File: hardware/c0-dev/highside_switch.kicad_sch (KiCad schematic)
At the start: 10 parts, among them U34 TPS26600PWP

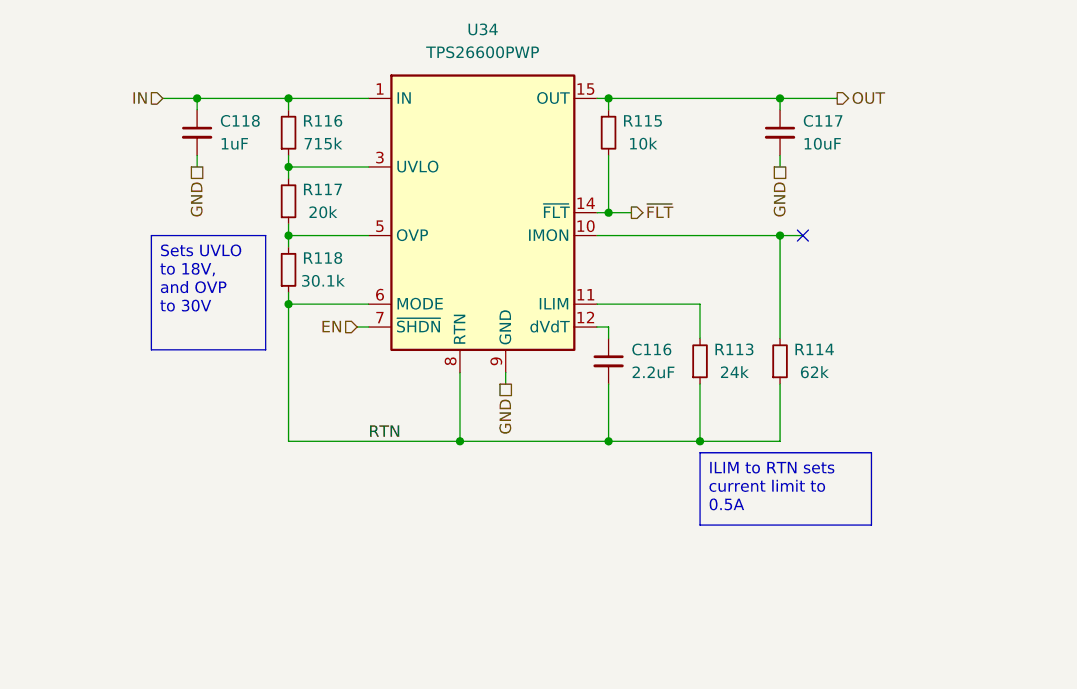
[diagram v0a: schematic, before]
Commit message: added DO
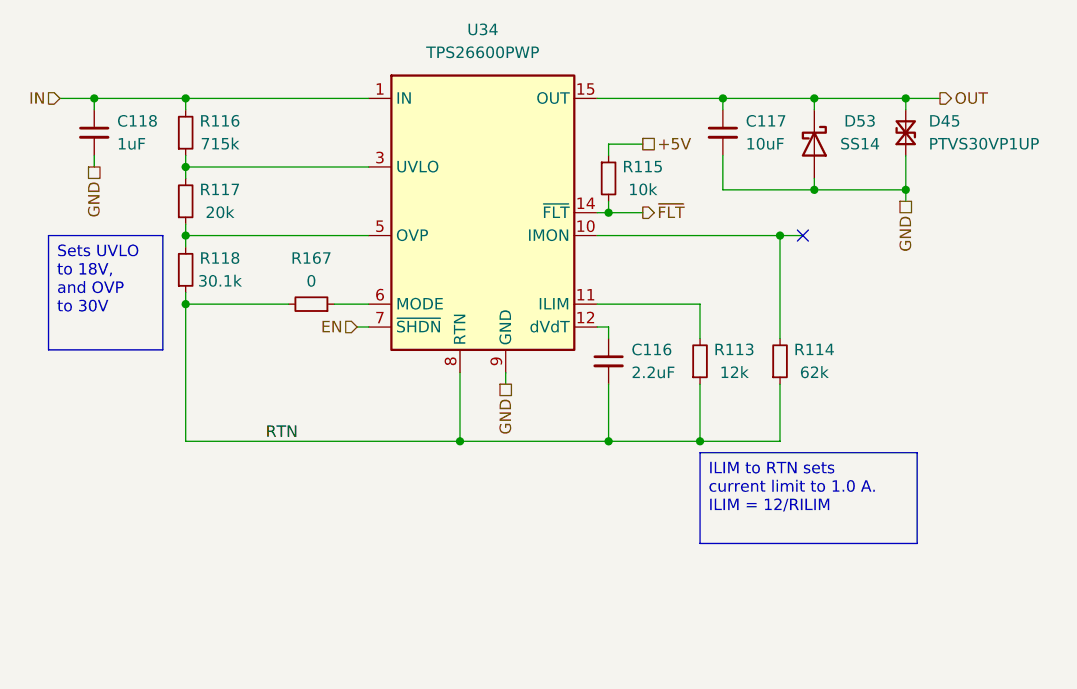
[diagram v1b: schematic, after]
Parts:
- added D45: PTVS30VP1UP, Diode_SMD:D_SOD-128, symbol Device:D_TVS_Small
- added D53: SS14, Diode_SMD:D_SMA, symbol Diode:B140-E3
- added R167: 0, Resistor_SMD:R_0402_1005Metric, symbol Device:R_Small
- R113: value 24k -> 12k
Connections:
- net GND: now also D45.1 (A1), D53.2 (A)
- net OUT: now also D45.2 (A2), D53.1 (K); no longer R115.1
- net RTN: now also R167.2; no longer U34.6 (MODE)
- new net: R167.1, U34.6 (MODE)
- new net +5V: R115.1
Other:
- moved on the sheet: C117, C118, R115, R116, R117, R118

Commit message: i2c address check
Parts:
- renumbered C118 to C122, C116 to C123, C117 to C124, D53 to D37, D45 to D38, R116 to R120, R117 to R121, R118 to R122, R167 to R123, R115 to R124, R113 to R125, R114 to R126, U34 to U36

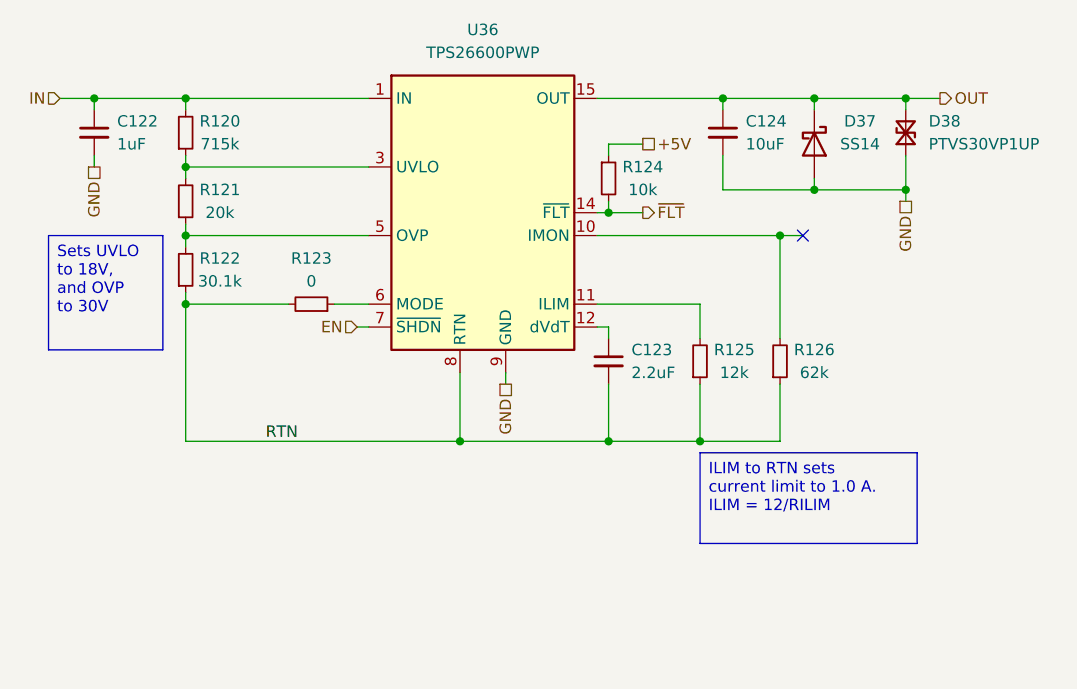
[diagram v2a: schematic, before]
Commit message: added connectors
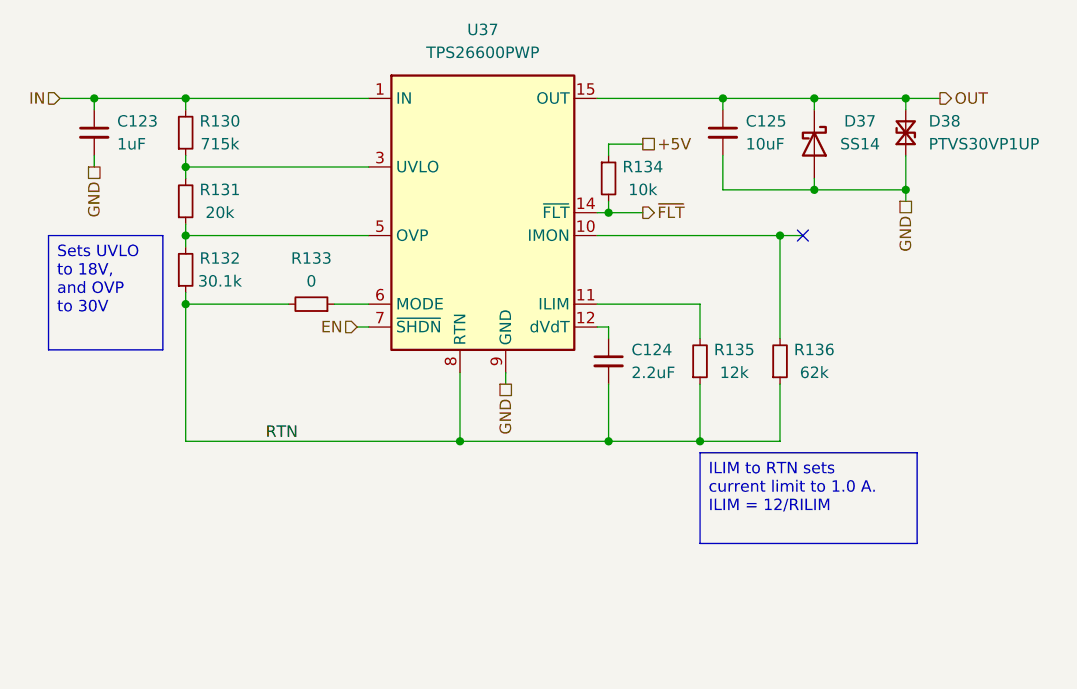
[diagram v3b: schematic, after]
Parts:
- renumbered C122 to C123, C123 to C124, C124 to C125, R120 to R130, R121 to R131, R122 to R132, R123 to R133, R124 to R134, R125 to R135, R126 to R136, U36 to U37

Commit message: added status leds
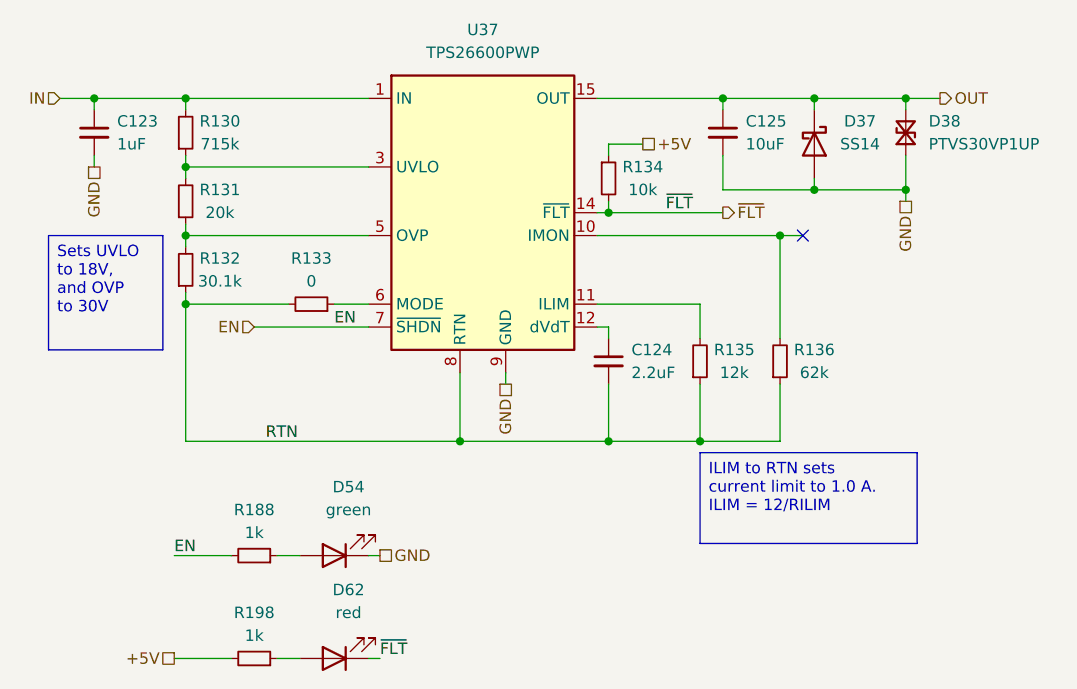
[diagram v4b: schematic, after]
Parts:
- added D54: green, LED_SMD:LED_0402_1005Metric, symbol Device:LED
- added D62: red, LED_SMD:LED_0402_1005Metric, symbol Device:LED
- added R188, R198: 1k, Resistor_SMD:R_0402_1005Metric, symbol Device:R_Small
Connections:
- net +5V: now also R198.2
- net EN: now also R188.2
- net GND: now also D54.1 (K)
- net ~{FLT}: now also D62.1 (K)
- new net: D62.2 (A), R198.1
- new net: D54.2 (A), R188.1

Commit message: added 4-pin connector
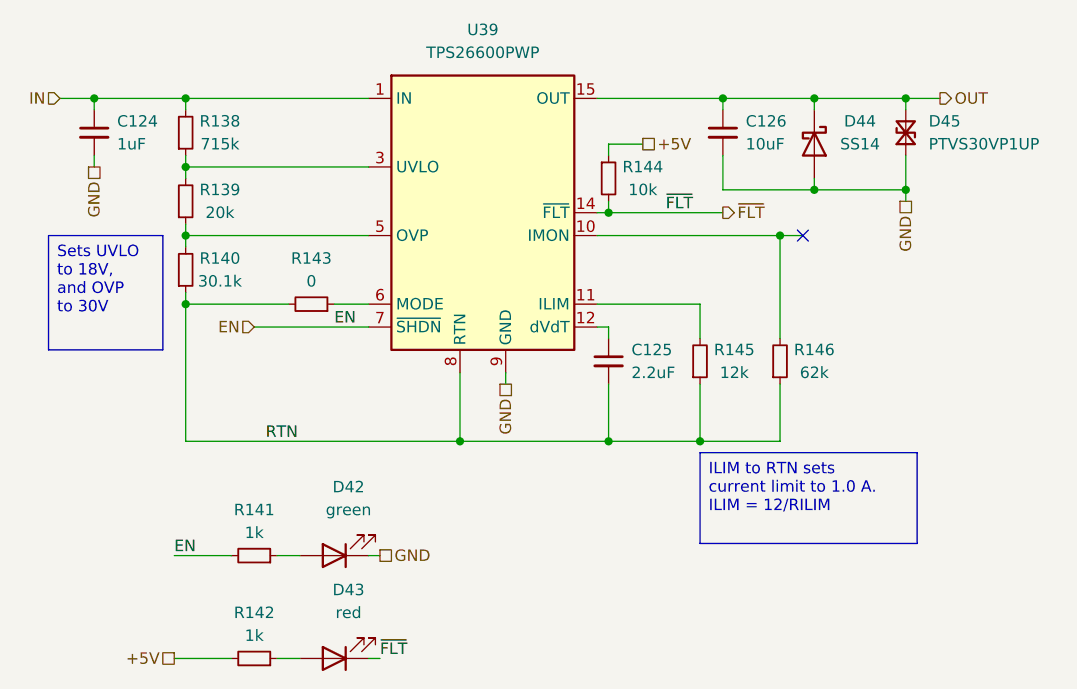
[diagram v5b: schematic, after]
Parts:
- renumbered C123 to C124, C124 to C125, C125 to C126, D54 to D42, D62 to D43, D37 to D44, D38 to D45, R130 to R138, R131 to R139, R132 to R140, R188 to R141, R198 to R142, R133 to R143, R134 to R144, R135 to R145, R136 to R146, U37 to U39

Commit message: annotation + new digital out
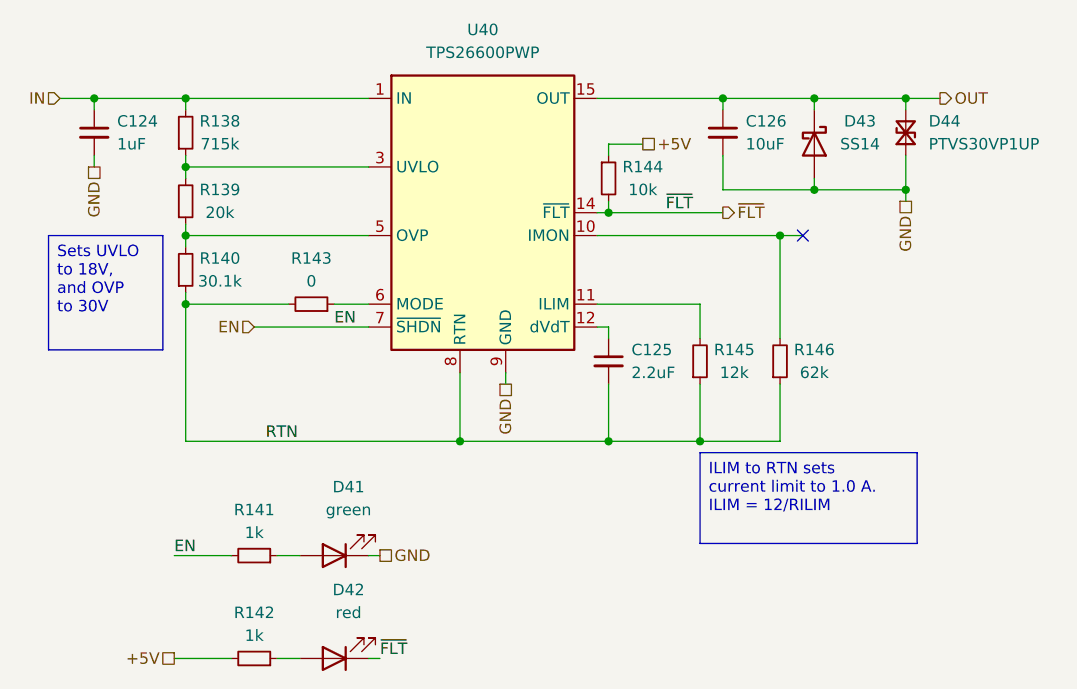
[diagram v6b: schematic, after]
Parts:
- renumbered D42 to D41, D43 to D42, D44 to D43, D45 to D44, U39 to U40
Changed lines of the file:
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@@
 		(dnp no)
 		(fields_autoplaced yes)
-		(property "Reference" "D43"
+		(property "Reference" "D42"
 			(at 101.9175 129.54 0)
 			(show_name no)
@@
 			(project "c0-dev"
 				(path "/b8347a0e-ad04-4414-969d-3c64a611d74e/680032e3-5da4-48ad-9c49-e468cbbeffb9/14d570e8-c412-49dd-bda0-6706a1bfd3e1"
-					(reference "D47")
+					(reference "D46")
 					(unit 1)
 				)
 				(path "/b8347a0e-ad04-4414-969d-3c64a611d74e/680032e3-5da4-48ad-9c49-e468cbbeffb9/3b235d4e-5dac-4c35-850e-dc45486b3878"
-					(reference "D55")
+					(reference "D54")
 					(unit 1)
 				)
 				(path "/b8347a0e-ad04-4414-969d-3c64a611d74e/680032e3-5da4-48ad-9c49-e468cbbeffb9/64747c64-021c-4a65-96a7-4b78a43ffa28"
-					(reference "D63")
+					(reference "D62")
 					(unit 1)
 				)
 				(path "/b8347a0e-ad04-4414-969d-3c64a611d74e/680032e3-5da4-48ad-9c49-e468cbbeffb9/8516472b-662a-48dd-8a8a-0634dd0851f0"
-					(reference "D71")
+					(reference "D70")
 					(unit 1)
 				)
 				(path "/b8347a0e-ad04-4414-969d-3c64a611d74e/680032e3-5da4-48ad-9c49-e468cbbeffb9/9a8c454e-897e-45d8-a464-57339f66e02b"
-					(reference "D59")
+					(reference "D58")
 					(unit 1)
 				)
 				(path "/b8347a0e-ad04-4414-969d-3c64a611d74e/680032e3-5da4-48ad-9c49-e468cbbeffb9/b5d4028a-660e-4e46-ac27-612085906853"
-					(reference "D51")
+					(reference "D50")
 					(unit 1)
 				)
 				(path "/b8347a0e-ad04-4414-969d-3c64a611d74e/680032e3-5da4-48ad-9c49-e468cbbeffb9/de5f394e-c667-494d-8bed-692ca82c493c"
-					(reference "D43")
+					(reference "D42")
 					(unit 1)
 				)
 				(path "/b8347a0e-ad04-4414-969d-3c64a611d74e/680032e3-5da4-48ad-9c49-e468cbbeffb9/e717e0e1-ea44-4eb2-9146-43919f8796f9"
-					(reference "D67")
+					(reference "D66")
 					(unit 1)
 				)
@@
 		(dnp no)
 		(fields_autoplaced yes)
-		(property "Reference" "D45"
+		(property "Reference" "D44"
 			(at 166.37 77.4699 90)
 			(show_name no)
@@
 			(project "c0-dev"
 				(path "/b8347a0e-ad04-4414-969d-3c64a611d74e/680032e3-5da4-48ad-9c49-e468cbbeffb9/14d570e8-c412-49dd-bda0-6706a1bfd3e1"
-					(reference "D49")
+					(reference "D48")
 					(unit 1)
 				)
 				(path "/b8347a0e-ad04-4414-969d-3c64a611d74e/680032e3-5da4-48ad-9c49-e468cbbeffb9/3b235d4e-5dac-4c35-850e-dc45486b3878"
-					(reference "D57")
+					(reference "D56")
 					(unit 1)
 				)
 				(path "/b8347a0e-ad04-4414-969d-3c64a611d74e/680032e3-5da4-48ad-9c49-e468cbbeffb9/64747c64-021c-4a65-96a7-4b78a43ffa28"
-					(reference "D65")
+					(reference "D64")
 					(unit 1)
 				)
 				(path "/b8347a0e-ad04-4414-969d-3c64a611d74e/680032e3-5da4-48ad-9c49-e468cbbeffb9/8516472b-662a-48dd-8a8a-0634dd0851f0"
-					(reference "D73")
+					(reference "D72")
 					(unit 1)
 				)
 				(path "/b8347a0e-ad04-4414-969d-3c64a611d74e/680032e3-5da4-48ad-9c49-e468cbbeffb9/9a8c454e-897e-45d8-a464-57339f66e02b"
-					(reference "D61")
+					(reference "D60")
 					(unit 1)
 				)
 				(path "/b8347a0e-ad04-4414-969d-3c64a611d74e/680032e3-5da4-48ad-9c49-e468cbbeffb9/b5d4028a-660e-4e46-ac27-612085906853"
-					(reference "D53")
+					(reference "D52")
 					(unit 1)
 				)
 				(path "/b8347a0e-ad04-4414-969d-3c64a611d74e/680032e3-5da4-48ad-9c49-e468cbbeffb9/de5f394e-c667-494d-8bed-692ca82c493c"
-					(reference "D45")
+					(reference "D44")
 					(unit 1)
 				)
 				(path "/b8347a0e-ad04-4414-969d-3c64a611d74e/680032e3-5da4-48ad-9c49-e468cbbeffb9/e717e0e1-ea44-4eb2-9146-43919f8796f9"
-					(reference "D69")
+					(reference "D68")
 					(unit 1)
 				)
@@
 		(dnp no)
 		(fields_autoplaced yes)
-		(property "Reference" "U39"
+		(property "Reference" "U40"
 			(at 116.84 67.31 0)
 			(show_name no)
@@
 			(project "c0-dev"
 				(path "/b8347a0e-ad04-4414-969d-3c64a611d74e/680032e3-5da4-48ad-9c49-e468cbbeffb9/14d570e8-c412-49dd-bda0-6706a1bfd3e1"
+					(reference "U41")
+					(unit 1)
+				)
+				(path "/b8347a0e-ad04-4414-969d-3c64a611d74e/680032e3-5da4-48ad-9c49-e468cbbeffb9/3b235d4e-5dac-4c35-850e-dc45486b3878"
+					(reference "U43")
+					(unit 1)
+				)
+				(path "/b8347a0e-ad04-4414-969d-3c64a611d74e/680032e3-5da4-48ad-9c49-e468cbbeffb9/64747c64-021c-4a65-96a7-4b78a43ffa28"
+					(reference "U45")
+					(unit 1)
+				)
+				(path "/b8347a0e-ad04-4414-969d-3c64a611d74e/680032e3-5da4-48ad-9c49-e468cbbeffb9/8516472b-662a-48dd-8a8a-0634dd0851f0"
+					(reference "U47")
+					(unit 1)
+				)
+				(path "/b8347a0e-ad04-4414-969d-3c64a611d74e/680032e3-5da4-48ad-9c49-e468cbbeffb9/9a8c454e-897e-45d8-a464-57339f66e02b"
+					(reference "U44")
+					(unit 1)
+				)
+				(path "/b8347a0e-ad04-4414-969d-3c64a611d74e/680032e3-5da4-48ad-9c49-e468cbbeffb9/b5d4028a-660e-4e46-ac27-612085906853"
+					(reference "U42")
+					(unit 1)
+				)
+				(path "/b8347a0e-ad04-4414-969d-3c64a611d74e/680032e3-5da4-48ad-9c49-e468cbbeffb9/de5f394e-c667-494d-8bed-692ca82c493c"
 					(reference "U40")
 					(unit 1)
 				)
-				(path "/b8347a0e-ad04-4414-969d-3c64a611d74e/680032e3-5da4-48ad-9c49-e468cbbeffb9/3b235d4e-5dac-4c35-850e-dc45486b3878"
-					(reference "U42")
-					(unit 1)
-				)
-				(path "/b8347a0e-ad04-4414-969d-3c64a611d74e/680032e3-5da4-48ad-9c49-e468cbbeffb9/64747c64-021c-4a65-96a7-4b78a43ffa28"
-					(reference "U44")
-					(unit 1)
-				)
-				(path "/b8347a0e-ad04-4414-969d-3c64a611d74e/680032e3-5da4-48ad-9c49-e468cbbeffb9/8516472b-662a-48dd-8a8a-0634dd0851f0"
+				(path "/b8347a0e-ad04-4414-969d-3c64a611d74e/680032e3-5da4-48ad-9c49-e468cbbeffb9/e717e0e1-ea44-4eb2-9146-43919f8796f9"
 					(reference "U46")
-					(unit 1)
-				)
-				(path "/b8347a0e-ad04-4414-969d-3c64a611d74e/680032e3-5da4-48ad-9c49-e468cbbeffb9/9a8c454e-897e-45d8-a464-57339f66e02b"
-					(reference "U43")
-					(unit 1)
-				)
-				(path "/b8347a0e-ad04-4414-969d-3c64a611d74e/680032e3-5da4-48ad-9c49-e468cbbeffb9/b5d4028a-660e-4e46-ac27-612085906853"
-					(reference "U41")
-					(unit 1)
-				)
-				(path "/b8347a0e-ad04-4414-969d-3c64a611d74e/680032e3-5da4-48ad-9c49-e468cbbeffb9/de5f394e-c667-494d-8bed-692ca82c493c"
-					(reference "U39")
-					(unit 1)
-				)
-				(path "/b8347a0e-ad04-4414-969d-3c64a611d74e/680032e3-5da4-48ad-9c49-e468cbbeffb9/e717e0e1-ea44-4eb2-9146-43919f8796f9"
-					(reference "U45")
 					(unit 1)
 				)
@@
 		(in_pos_files yes)
 		(dnp no)
-		(property "Reference" "D44"
+		(property "Reference" "D43"
 			(at 158.75 77.47 90)
 			(show_name no)
@@
 			(project "c0-dev"
 				(path "/b8347a0e-ad04-4414-969d-3c64a611d74e/680032e3-5da4-48ad-9c49-e468cbbeffb9/14d570e8-c412-49dd-bda0-6706a1bfd3e1"
-					(reference "D48")
+					(reference "D47")
 					(unit 1)
 				)
 				(path "/b8347a0e-ad04-4414-969d-3c64a611d74e/680032e3-5da4-48ad-9c49-e468cbbeffb9/3b235d4e-5dac-4c35-850e-dc45486b3878"
-					(reference "D56")
+					(reference "D55")
 					(unit 1)
 				)
 				(path "/b8347a0e-ad04-4414-969d-3c64a611d74e/680032e3-5da4-48ad-9c49-e468cbbeffb9/64747c64-021c-4a65-96a7-4b78a43ffa28"
-					(reference "D64")
+					(reference "D63")
 					(unit 1)
 				)
 				(path "/b8347a0e-ad04-4414-969d-3c64a611d74e/680032e3-5da4-48ad-9c49-e468cbbeffb9/8516472b-662a-48dd-8a8a-0634dd0851f0"
-					(reference "D72")
+					(reference "D71")
 					(unit 1)
 				)
 				(path "/b8347a0e-ad04-4414-969d-3c64a611d74e/680032e3-5da4-48ad-9c49-e468cbbeffb9/9a8c454e-897e-45d8-a464-57339f66e02b"
-					(reference "D60")
+					(reference "D59")
 					(unit 1)
 				)
 				(path "/b8347a0e-ad04-4414-969d-3c64a611d74e/680032e3-5da4-48ad-9c49-e468cbbeffb9/b5d4028a-660e-4e46-ac27-612085906853"
-					(reference "D52")
+					(reference "D51")
 					(unit 1)
 				)
 				(path "/b8347a0e-ad04-4414-969d-3c64a611d74e/680032e3-5da4-48ad-9c49-e468cbbeffb9/de5f394e-c667-494d-8bed-692ca82c493c"
-					(reference "D44")
+					(reference "D43")
 					(unit 1)
 				)
 				(path "/b8347a0e-ad04-4414-969d-3c64a611d74e/680032e3-5da4-48ad-9c49-e468cbbeffb9/e717e0e1-ea44-4eb2-9146-43919f8796f9"
-					(reference "D68")
+					(reference "D67")
 					(unit 1)
 				)
@@
 		(dnp no)
 		(fields_autoplaced yes)
-		(property "Reference" "D42"
+		(property "Reference" "D41"
 			(at 101.9175 118.11 0)
 			(show_name no)
@@
 			(project "c0-dev"
 				(path "/b8347a0e-ad04-4414-969d-3c64a611d74e/680032e3-5da4-48ad-9c49-e468cbbeffb9/14d570e8-c412-49dd-bda0-6706a1bfd3e1"
-					(reference "D46")
+					(reference "D45")
 					(unit 1)
 				)
 				(path "/b8347a0e-ad04-4414-969d-3c64a611d74e/680032e3-5da4-48ad-9c49-e468cbbeffb9/3b235d4e-5dac-4c35-850e-dc45486b3878"
-					(reference "D54")
+					(reference "D53")
 					(unit 1)
 				)
 				(path "/b8347a0e-ad04-4414-969d-3c64a611d74e/680032e3-5da4-48ad-9c49-e468cbbeffb9/64747c64-021c-4a65-96a7-4b78a43ffa28"
-					(reference "D62")
+					(reference "D61")
 					(unit 1)
 				)
 				(path "/b8347a0e-ad04-4414-969d-3c64a611d74e/680032e3-5da4-48ad-9c49-e468cbbeffb9/8516472b-662a-48dd-8a8a-0634dd0851f0"
-					(reference "D70")
+					(reference "D69")
 					(unit 1)
 				)
 				(path "/b8347a0e-ad04-4414-969d-3c64a611d74e/680032e3-5da4-48ad-9c49-e468cbbeffb9/9a8c454e-897e-45d8-a464-57339f66e02b"
-					(reference "D58")
+					(reference "D57")
 					(unit 1)
 				)
 				(path "/b8347a0e-ad04-4414-969d-3c64a611d74e/680032e3-5da4-48ad-9c49-e468cbbeffb9/b5d4028a-660e-4e46-ac27-612085906853"
-					(reference "D50")
+					(reference "D49")
 					(unit 1)
 				)
 				(path "/b8347a0e-ad04-4414-969d-3c64a611d74e/680032e3-5da4-48ad-9c49-e468cbbeffb9/de5f394e-c667-494d-8bed-692ca82c493c"
-					(reference "D42")
+					(reference "D41")
 					(unit 1)
 				)
 				(path "/b8347a0e-ad04-4414-969d-3c64a611d74e/680032e3-5da4-48ad-9c49-e468cbbeffb9/e717e0e1-ea44-4eb2-9146-43919f8796f9"
-					(reference "D66")
-					(unit 1)
-				)
+					(reference "D65")
+					(unit 1)
+				)
